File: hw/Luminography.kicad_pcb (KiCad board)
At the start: 2 copper layers, 100 x 100 mm, 109 parts, among them J1 USB_C_Receptacle_PowerOnly_6P, J2 Conn_01x04, Q1 MMBT3904, Q2 2N7002, SW1 SW_Push, U1 LTC4054ES5-4.2, U100 BH1750FVI-TR, U101 BH1750FVI-TR, U102 BH1750FVI-TR, U103 BH1750FVI-TR, U104 BH1750FVI-TR, U105 BH1750FVI-TR, U106 BH1750FVI-TR, U107 BH1750FVI-TR, U108 BH1750FVI-TR, U109 BH1750FVI-TR, U110 BH1750FVI-TR, U111 BH1750FVI-TR, U112 BH1750FVI-TR, U113 BH1750FVI-TR, U114 BH1750FVI-TR, U115 BH1750FVI-TR, U116 BH1750FVI-TR, U117 BH1750FVI-TR, U118 BH1750FVI-TR, U119 BH1750FVI-TR, U120 BH1750FVI-TR, U121 BH1750FVI-TR, U122 BH1750FVI-TR, U123 BH1750FVI-TR, U2 XS3A1T3157GMX, U3 SPX3819M5-L-3-3, U4 MAX17048G+T10, U5 STM32G030K6Tx, U6 ZJY128R-IG01, U7 BMI270, U8 MMC5603NJ, U9 MAX98357AETE+, X1 12.288MHz

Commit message: 🚧 Layout WIP
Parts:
- removed D3: White, LED_SMD:LED_0603_1608Metric
- removed R13: 7.5k, Resistor_SMD:R_0402_1005Metric
- added C11: 100n, Capacitor_SMD:C_0402_1005Metric, F.Cu at (26.8, 62.3)
- added U7: W25Q16JVUXIQ, W25Q16JVUXIQ:SON50P300X200X60-9N, F.Cu at (27.9, 59.7)
- moved Q2 114.5 mm to (95.6, 106.8), turned to -90 degrees
- moved C9 94.0 mm to (99.2, 108.2)
- moved R4 92.8 mm to (-26.3, 36.8), turned to 90 degrees
- moved R9 92.3 mm to (97.8, 107.8), turned to 90 degrees
- moved R3 92.2 mm to (-25.8, 33.5)
- moved D2 90.9 mm to (-23.4, 33.4), turned to 180 degrees
- moved R10 88.7 mm to (97.8, 105.9), turned to 90 degrees
- moved R6 85.2 mm to (-16.3, 13.0), turned to -90 degrees
- moved R2 84.5 mm to (-16.0, 45.4), turned to 180 degrees
- moved R5 84.3 mm to (-16.3, 15.0), turned to -90 degrees
- moved R1 83.2 mm to (-14.1, 45.4)
- moved C1 82.6 mm to (-26.3, 34.9), turned to -90 degrees
- moved R7 82.0 mm to (-14.4, 20.6)
- moved D1 80.2 mm to (-22.7, 49.6), turned to -90 degrees
- moved C2 77.3 mm to (-21.1, 35.4), turned to -90 degrees
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- renumbered C15 to C10, C9 to C12, C10 to C13, C11 to C14, C12 to C15, C13 to C16, C14 to C9, U9 to U10, U7 to U8, U8 to U9
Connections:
- U5 pad 19: I2Cx_SCL -> SPI_MISO
- U5 pad 20: unconnected-(U5-PC6-Pad20) -> FLASH_CS
- U5 pad 21: ACT_LED -> I2Cx_SCL
- U5 pad 22: unconnected-(U5-PA11/PA9-Pad22) -> PWR_LATCH

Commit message: 🚧 Routing WIP
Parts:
- removed the Q1 at (-14.2, 14.0)
- removed the R5 at (-16.3, 15.0)
- added R12: 1k, Resistor_SMD:R_0402_1005Metric, F.Cu at (111.1, 107.0)
- added R6: 1M, Resistor_SMD:R_0402_1005Metric, F.Cu at (143.7, 103.0)
- added SW2: SW_Push, Button_Switch_SMD:SW_SPST_TL3342, B.Cu at (140.0, 100.0)
- R5: renamed from R6; value 30k -> 1M
- SW1: moved to B.Cu
- moved U2 161.8 mm to (98.0, 137.7)
- moved R7 161.1 mm to (97.8, 136.3), turned to 180 degrees
- moved C3 159.2 mm to (103.9, 136.8)
- moved C4 159.2 mm to (103.9, 135.0)
- moved U3 159.2 mm to (101.3, 135.9)
- moved C1 155.5 mm to (90.3, 137.9)
- moved C2 155.5 mm to (95.5, 138.3)
- moved D2 155.5 mm to (93.2, 136.3)
- moved R3 155.5 mm to (90.8, 136.5)
- moved U1 155.5 mm to (92.9, 138.8)
- moved R4 155.5 mm to (90.3, 139.7)
- moved U4 151.3 mm to (101.9, 138.9)
- moved C5 151.3 mm to (99.7, 139.0)
- moved J1 149.0 mm to (99.6, 144.9)
- moved R1 149.0 mm to (100.5, 140.5)
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- renumbered Q2 to Q1, R12 to R13
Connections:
- R5 pad 1: VDD -> BTNA_INTR
- R5 pad 2: BTN_INTR -> GND
- SW1 pad 2: Net-(U2-Y1) -> BTNA_INTR
- U2 pad 3: Net-(U2-Y1) -> BTNA_INTR
- U5 pad 1: LCD_RSTN -> LCD_CS
- U5 pad 22: PWR_LATCH -> BTNA_INTR
- U5 pad 24: SWDIO -> BTNB_INTR
- U5 pad 3: BMI_CS -> PWR_LATCH
- U5 pad 30: LCD_CS -> LCD_RSTN
- U8 pad 1: unconnected-(U8-SDO-Pad1) -> GND
- U8 pad 12: BMI_CS -> VDD
- U8 pad 13: SPI_SCK -> I2Cx_SCL
- U8 pad 14: SPI_MOSI -> I2Cx_SDA_00
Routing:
- net VDD: track 280.4 -> 417.8 mm, vias 24 -> 33
- net BTNA_INTR: track 0.00 -> 97.2 mm, vias 0 -> 5
- net VBAT: track 0.00 -> 66.2 mm, vias 0 -> 3
- net BTNB_INTR: track 0.00 -> 44.8 mm, vias 0 -> 3
- net GND: track 6.00 -> 46.5 mm, vias 24 -> 60
- net I2Cx_SCL: track 290.4 -> 322.4 mm, vias 24 -> 27
- net PWR_LATCH: track 0.00 -> 31.1 mm, vias 0 -> 2
- net SPI_SCK: track 0.00 -> 30.6 mm, vias 0 -> 2
- net SPI_MOSI: track 0.00 -> 26.8 mm, vias 0 -> 2
- net VBUS: track 0.00 -> 20.8 mm
- net LCD_BL: track 0.00 -> 15.4 mm
- net LCD_CS: track 0.00 -> 13.5 mm
- net LCD_DC: track 0.00 -> 13.0 mm
- net BH1750FVI_DVI: track 272.5 -> 283.5 mm, vias 2 -> 24
- net LCD_RSTN: track 0.00 -> 10.3 mm
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- added copper zone on B.Cu, net GND
- added copper zone on F.Cu, net GND
- added copper zone on F.Cu, net Net-(X1-EN)
- added copper zone on F.Cu, net VDD

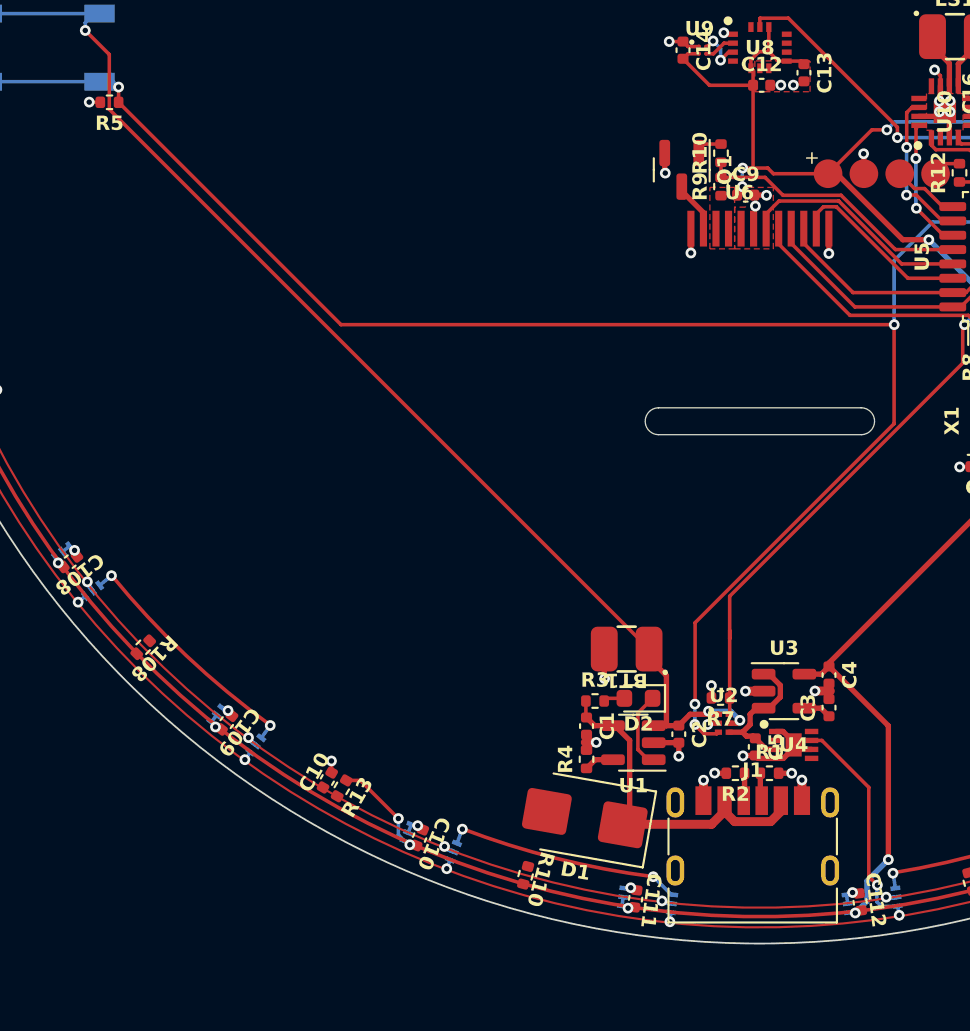
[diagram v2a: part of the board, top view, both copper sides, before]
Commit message: 🚧 Change USB receptacle to a fully surface-mount model
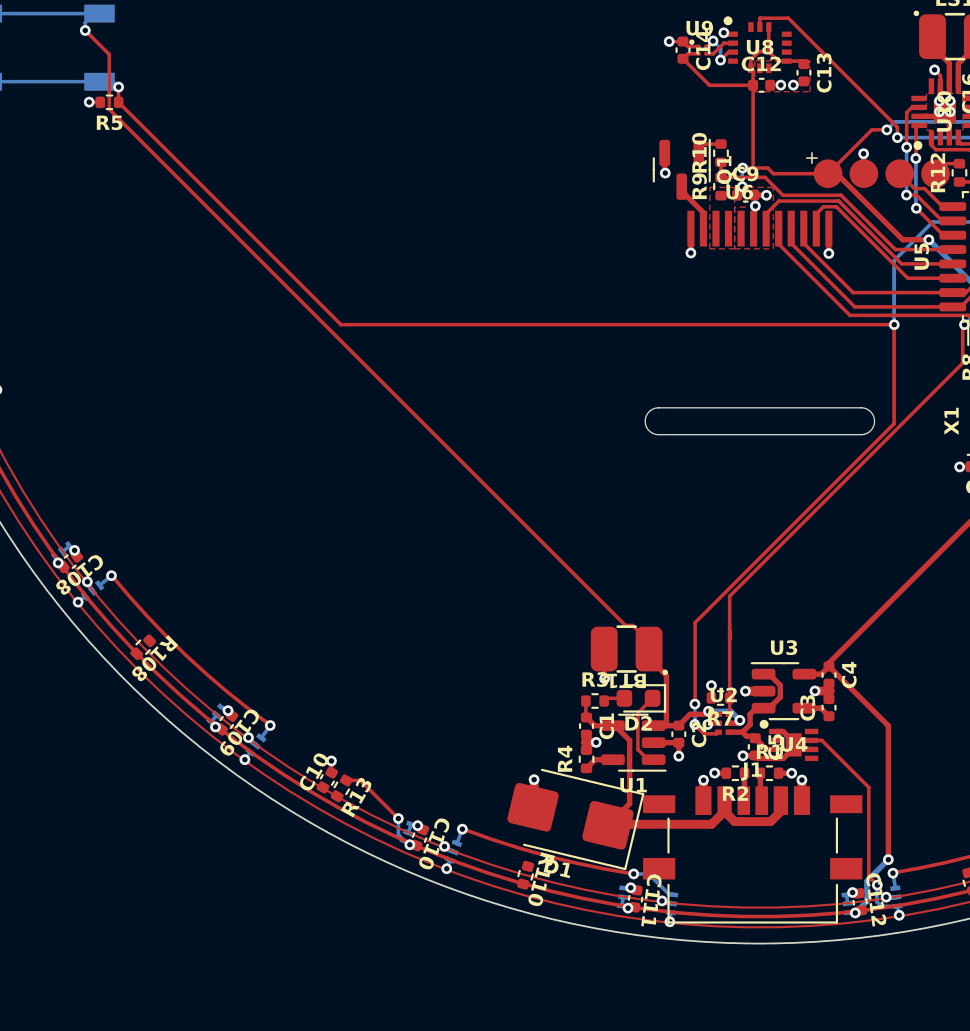
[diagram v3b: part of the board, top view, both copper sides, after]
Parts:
- moved D1 0.81 mm to (89.4, 142.9), turned to 166.5 degrees
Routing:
- net GND: track 46.5 -> 48.1 mm, vias 60 -> 61
- net VBUS: track 20.8 -> 21.4 mm
